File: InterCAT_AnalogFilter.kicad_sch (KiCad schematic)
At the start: 39 parts, among them T1 LM-NP-1001-B1L, T2 LM-NP-1001-B1L, T3 LM-NP-1001-B1L, T4 LM-NP-1001-B1L, U4 MCP6002, U5 MCP6002, U6 MCP6002

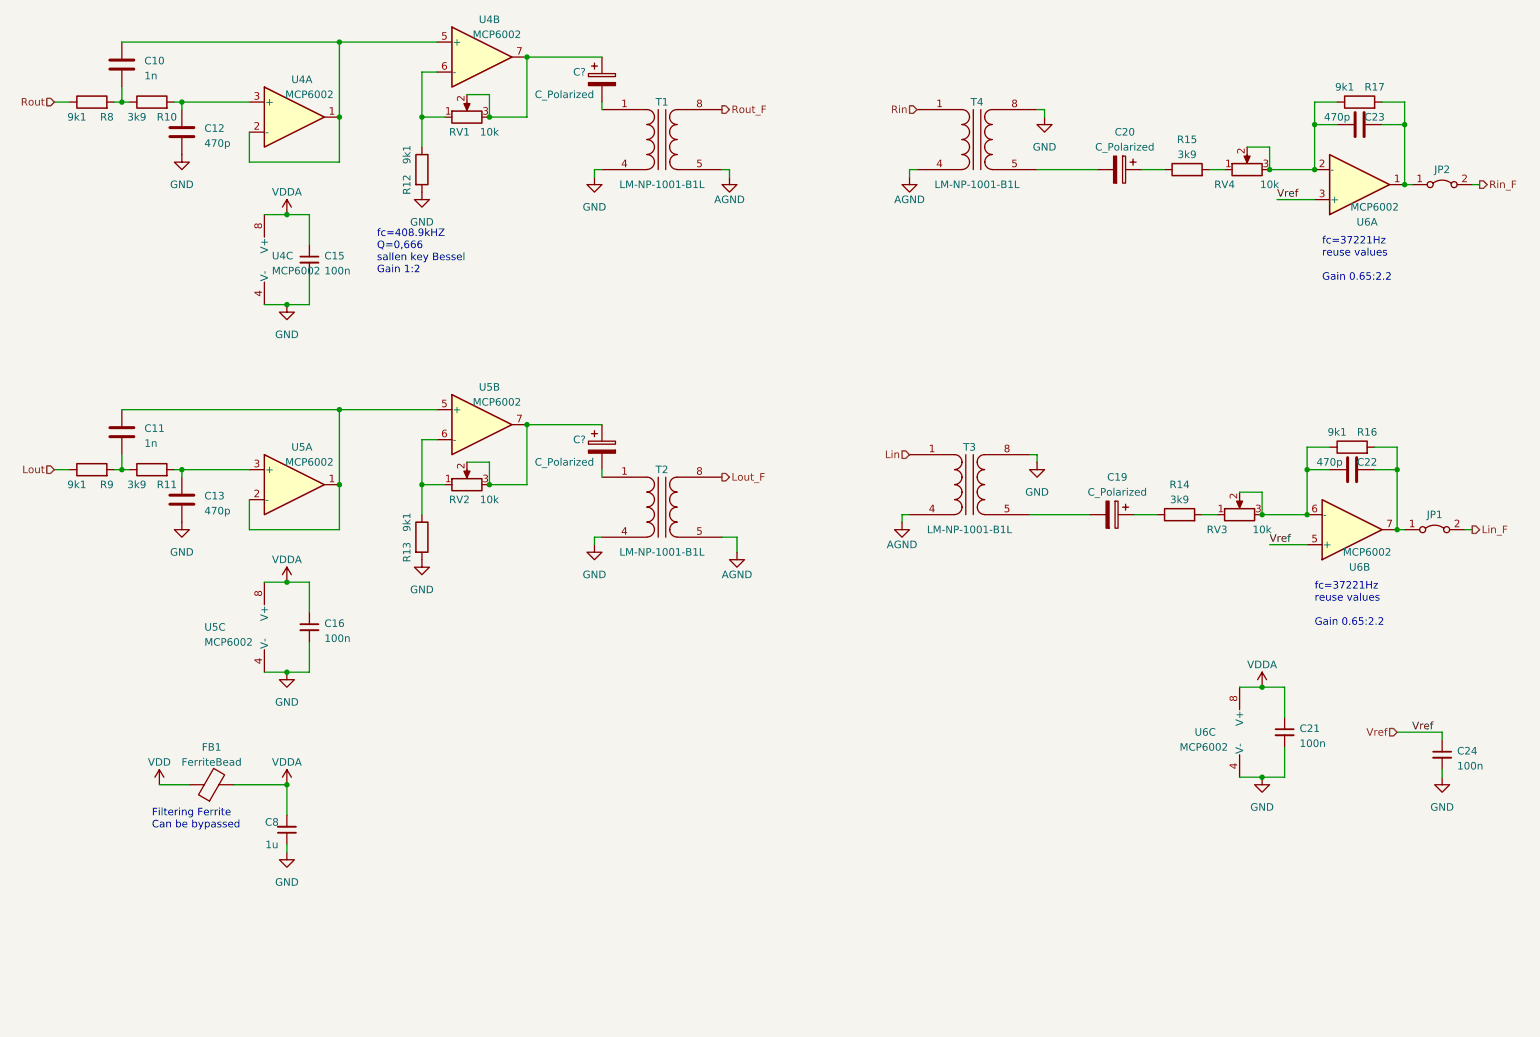
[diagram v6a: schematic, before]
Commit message: changed schematic to full mono
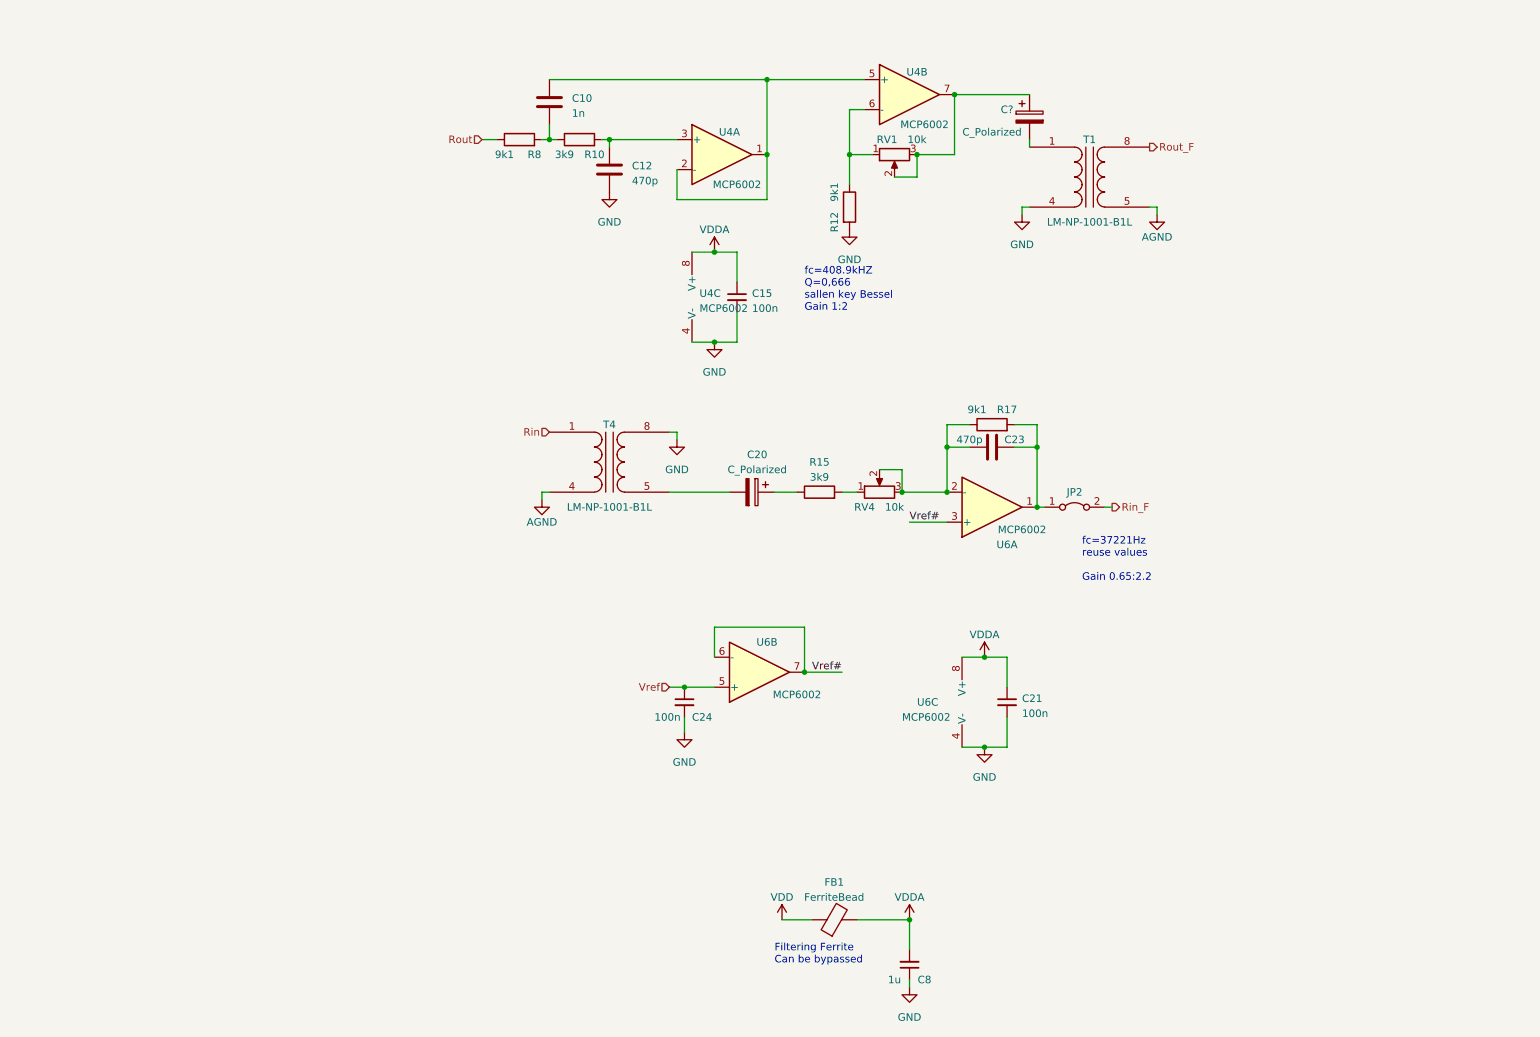
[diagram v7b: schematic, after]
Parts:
- removed C11: 1n, Capacitor_SMD:C_0603_1608Metric, symbol Device:C
- removed C13, C22: 470p, Capacitor_SMD:C_0603_1608Metric, symbol Device:C
- removed C16: 100n, Capacitor_SMD:C_0603_1608Metric, symbol Device:C_Small
- removed C19, C?: C_Polarized, Capacitor_THT:CP_Radial_D5.0mm_P2.50mm, symbol Device:C_Polarized
- removed JP1: Jumper_2_Bridged, Jumper:SolderJumper-2_P1.3mm_Bridged_RoundedPad1.0x1.5mm, symbol Jumper:Jumper_2_Bridged
- removed R11, R14: 3k9, Resistor_SMD:R_0603_1608Metric, symbol Device:R
- removed R13, R16, R9: 9k1, Resistor_SMD:R_0603_1608Metric, symbol Device:R
- removed RV2, RV3: 10k, Potentiometer_THT:Potentiometer_Bourns_3386P_Vertical, symbol Device:R_Potentiometer
- removed T2, T3: LM-NP-1001-B1L, InterCat:LM-NP-1001-B1L, symbol InterCat:LM-NP-1001-B1L
- removed U5: MCP6002, Package_SO:SOIC-8_3.9x4.9mm_P1.27mm, symbol Amplifier_Operational:TL082
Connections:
- net Vref: no longer U6.3 (+)
- net Vref#: now reaches U6.6 (-)
- net Vref#: now also U6.3 (+), U6.7
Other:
- moved on the sheet: C10, C12, C15, C20, C21, C23, C24, C8, C?, FB1, JP2, R10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

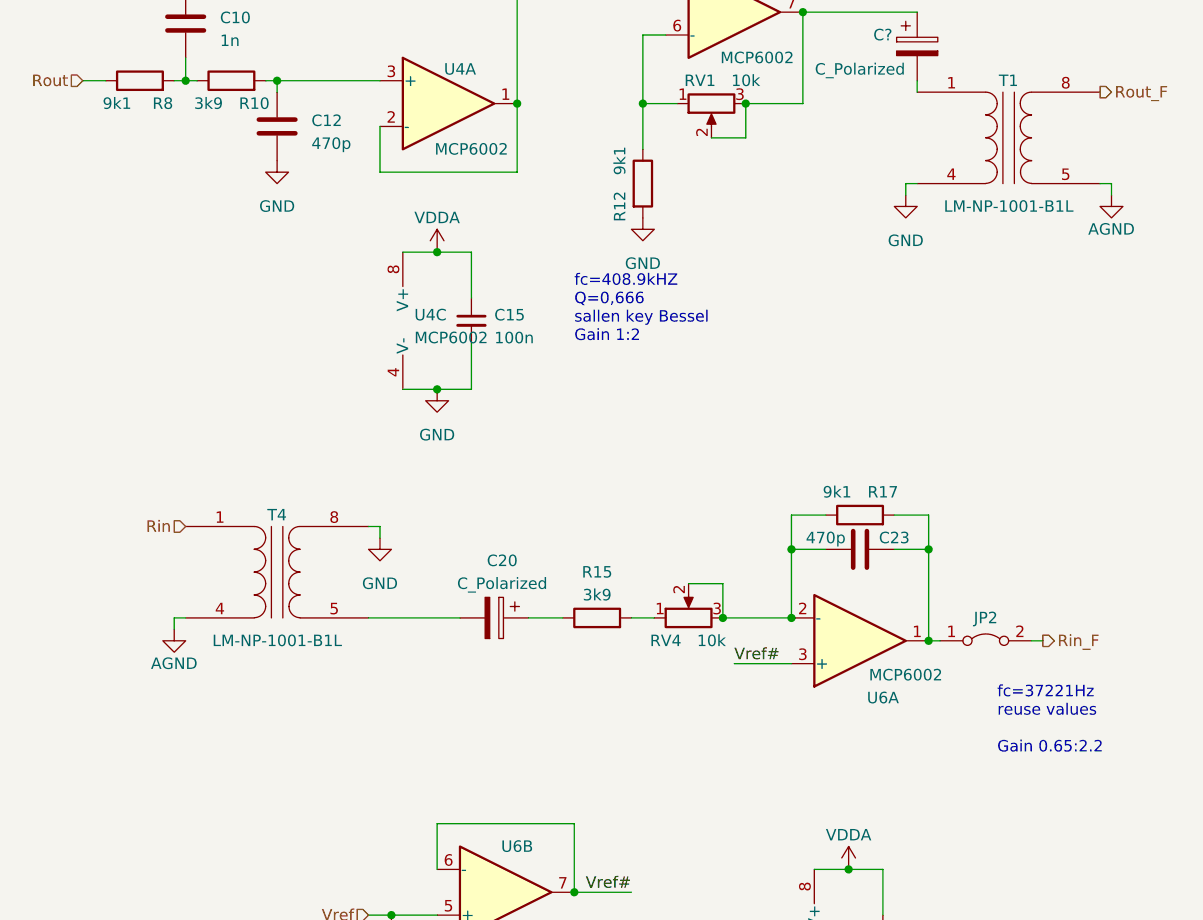
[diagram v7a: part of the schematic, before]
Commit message: redone analog channels to improve dynamic range, removed DC block
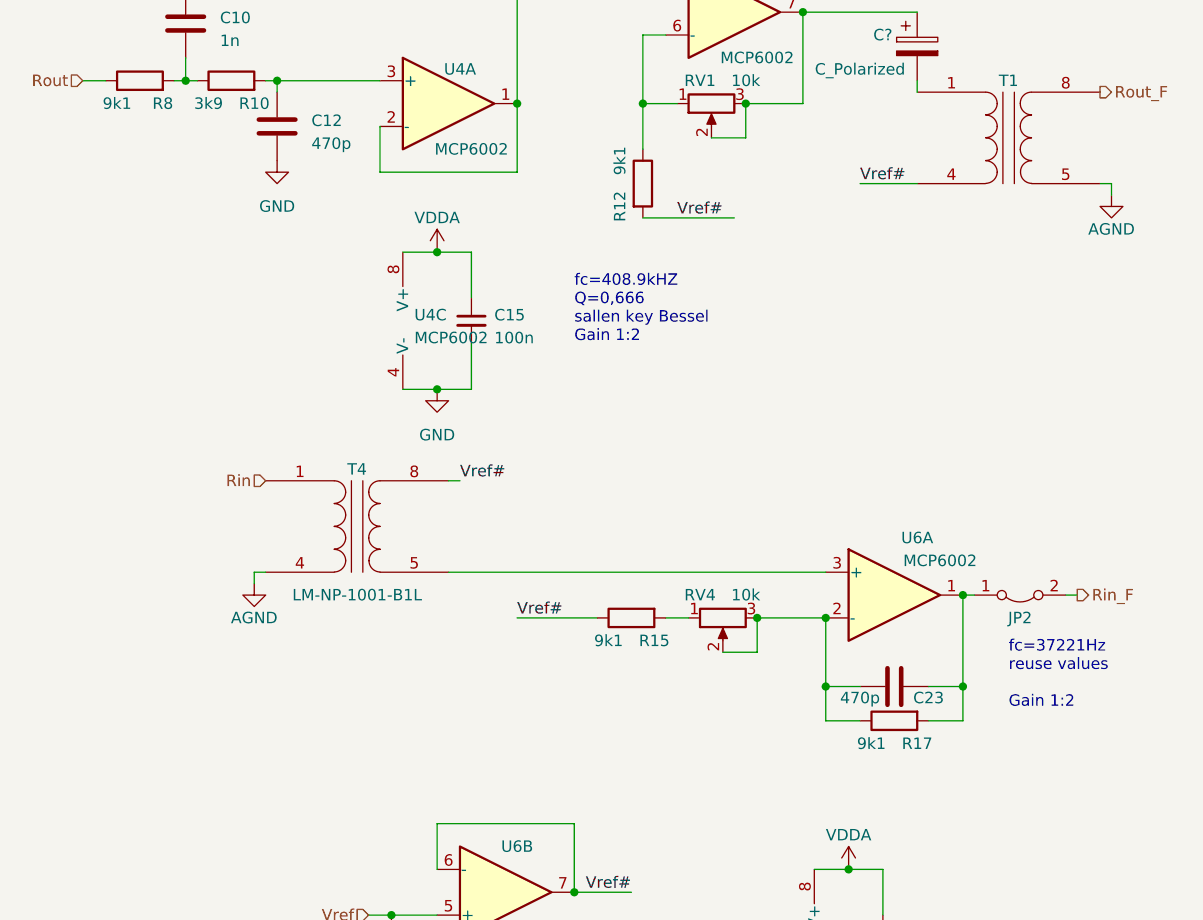
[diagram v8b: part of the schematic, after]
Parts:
- removed C20: C_Polarized, Capacitor_THT:CP_Radial_D5.0mm_P2.50mm, symbol Device:C_Polarized
- R15: value 3k9 -> 9k1; LCSC C23018 -> C23260
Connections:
- net GND: no longer R12.2, T1.4 (AB), T4.8 (SB)
- net Vref#: now also R12.2, R15.1, T1.4 (AB), T4.8 (SB); no longer U6.3 (+)
- net at T4.5 (SA): now also U6.3 (+)
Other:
- note added: "fc=37221Hz reuse values Gain 1:2"
- note removed: "fc=37221Hz reuse values Gain 0.65:2.2"
- moved on the sheet: C23, JP2, R17, RV4, T4, U6A
